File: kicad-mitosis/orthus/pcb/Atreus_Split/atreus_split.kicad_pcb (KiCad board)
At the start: 2 copper layers, 133.4 x 111.4 mm, 34 parts, among them J1 Conn_01x04, Q1 Si2302, Q2 Si2302

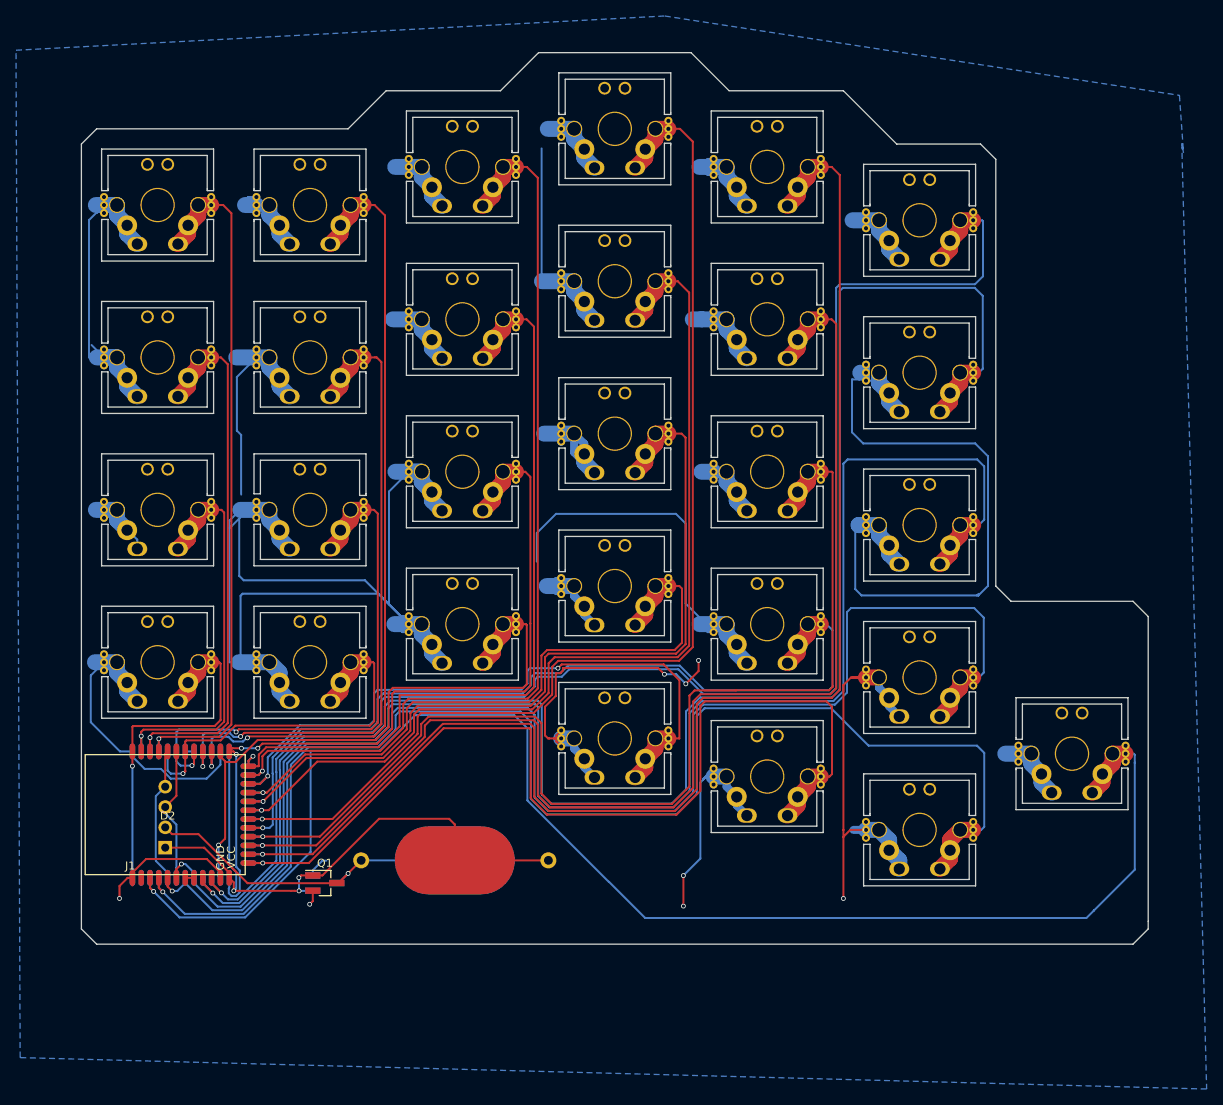
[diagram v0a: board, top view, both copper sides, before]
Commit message: change key position, clean up
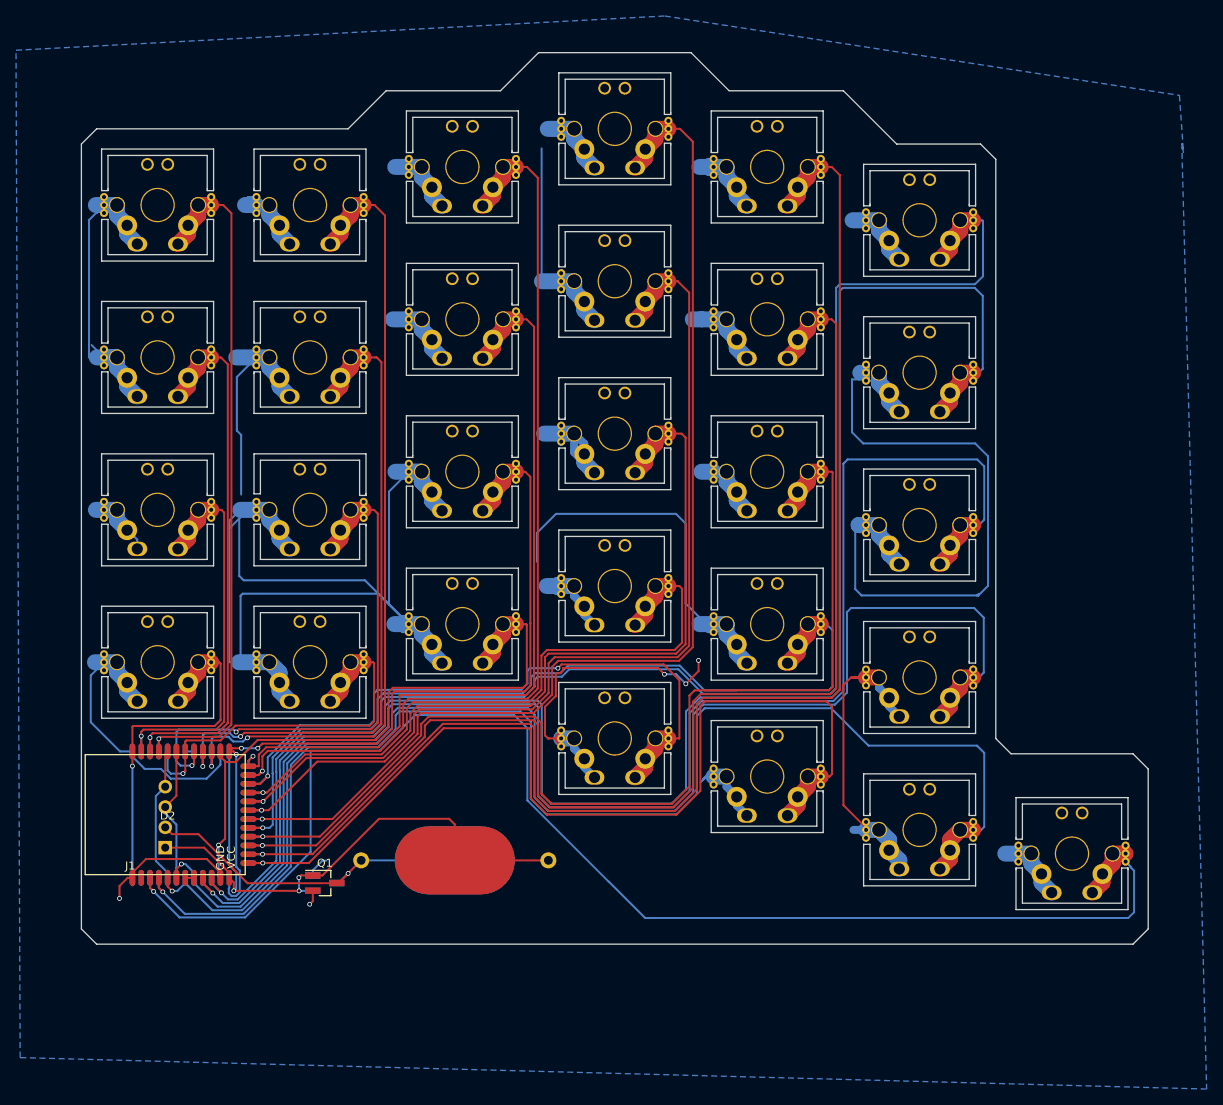
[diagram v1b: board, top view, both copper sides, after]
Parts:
- moved S71 12.5 mm to (152.4, 119.2)
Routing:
- net GND: track 809.6 -> 784.3 mm, vias 8 -> 5
- net /S71: track 189.1 -> 178.0 mm
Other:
- outline, holes or cut-outs redrawn
